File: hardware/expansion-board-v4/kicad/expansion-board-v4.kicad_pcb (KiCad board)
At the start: 6 copper layers, 100 x 62 mm, 174 parts, among them J1 PinHeader_2x20_P2.54mm_Vertic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, J2 U.FL_Hirose_U.FL-R-SMT-1_Vert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, J4 USB_C_Receptacle_HRO_TYPE-C-3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, J5 U.FL_Hirose_U.FL-R-SMT-1_Vert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, J6 U.FL_Hirose_U.FL-R-SMT-1_Vert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, J7 U.FL_Hirose_U.FL-R-SMT-1_Vert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, J8 U.FL_Hirose_U.FL-R-SMT-1_Vert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, J9 MX1.25WT-2P, Q2 SOT-23, Q3 SOT-23, Q4 SOT-23, Q5 SOT-23, SW2 SolderJumper-2_P1.3mm_Open_Pa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, U1 SOT-23-5, U10 QFN-48-1EP_7x7mm_P0.5mm_EP5.1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, U11 DFN-8-1EP_2x2mm_P0.5mm_EP0.86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, U12 SOT-363_SC-70-6, U14 MSOP-8_3x3mm_P0.65mm, U15 SOT-23-6, U16 SOT-363_SC-70-6, U17 SOT-363_SC-70-6, U18 SOIC-10_3.9x4.9mm_P1mm, U19 QFN-24-1EP_4x4mm_P0.5mm_EP2.6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, U2 SOT-23-5, U20 TSOT-23-6, U3 SOT-23-5, U4 BNO085_LGA-28, U5 BMP388_LGA-10, U6 LGA-16_3x3mm_P0.5mm, U7 ATGM336H_LCC-18, U8 QFN-56-1EP_7x7mm_P0.4mm_EP3.2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, U9 SOIC-8_5.3x5.3mm_P1.27mm, Y1 Crystal_SMD_3225-4Pin_3.2x2.5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, Y2 Crystal_SMD_3225-4Pin_3.2x2.5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, Y3 Crystal_SMD_3215-2Pin_3.2x1.5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

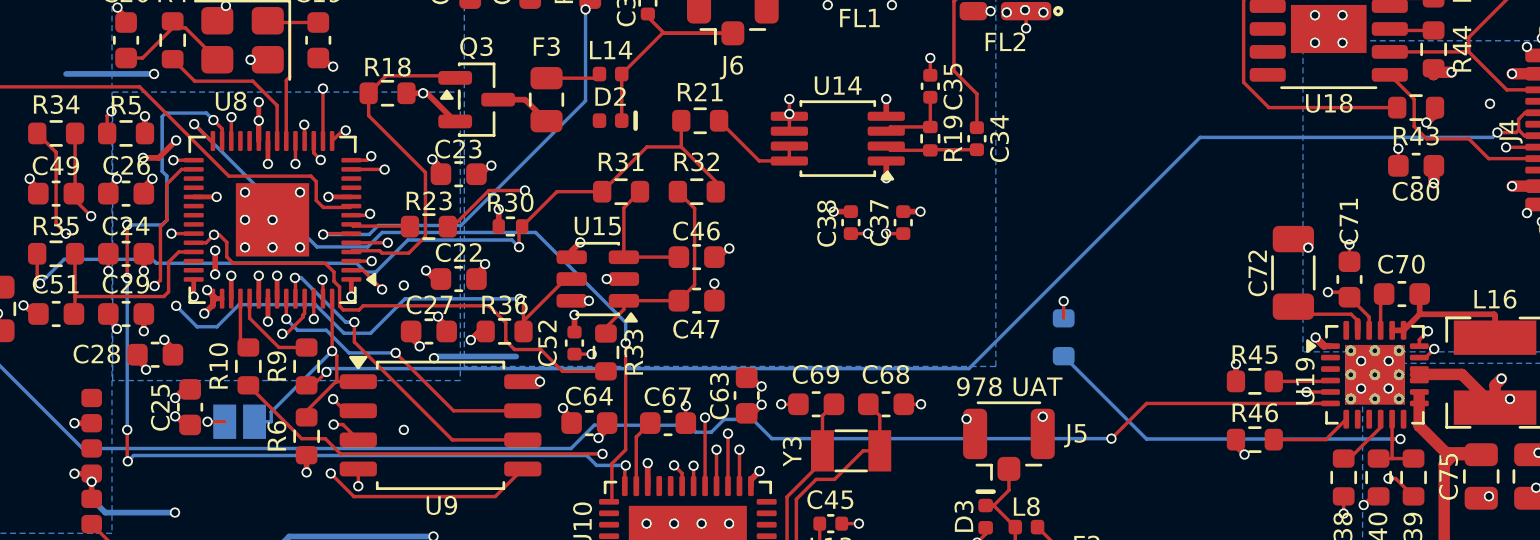
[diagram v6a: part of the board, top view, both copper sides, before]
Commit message: chore(v4): 固化——八维度 1:1 复现通过
从固化数据走完整重建链（gen_pcb → import_routes → route_ifa_feed →
silk_texts → silk_size → gen_polarity_marks → enforce_via_spec），
与手上这块板逐维度比对：

    元件       174 / 174   ✅      覆铜区      15 /  15   ✅
    位号       174 / 174   ✅      板级图元    26 /  26   ✅
    走线      1250 /1250   ✅      封装丝印   174 / 174   ✅
    过孔       385 / 385   ✅      焊盘钻孔   174 / 174   ✅
    未连通       0 /   0   ✅

走线/过孔的差异只有 1~50nm（KiCad 内部单位就是 1nm，制造分辨率是 µm）。

本轮板子改动：
· U19 EP 的 9 个 via-in-pad 钻孔 0.20 → 0.30mm（环宽 0.100mm）
· 删掉我之前多加的 4 个 EP 过孔——9 个 0.3mm 的 3×3 阵列已经够，
  13 个孔挤在 2.6mm EP 里过密
· RP_1V1 两条桥接线按可用上限收到 0.47 / 0.22mm
  （其中一条被 SUBG_RESET 过孔卡死，DRC 报 0.0495mm 间距）
· CHG_PMID 采纳罩哥的 0.25mm
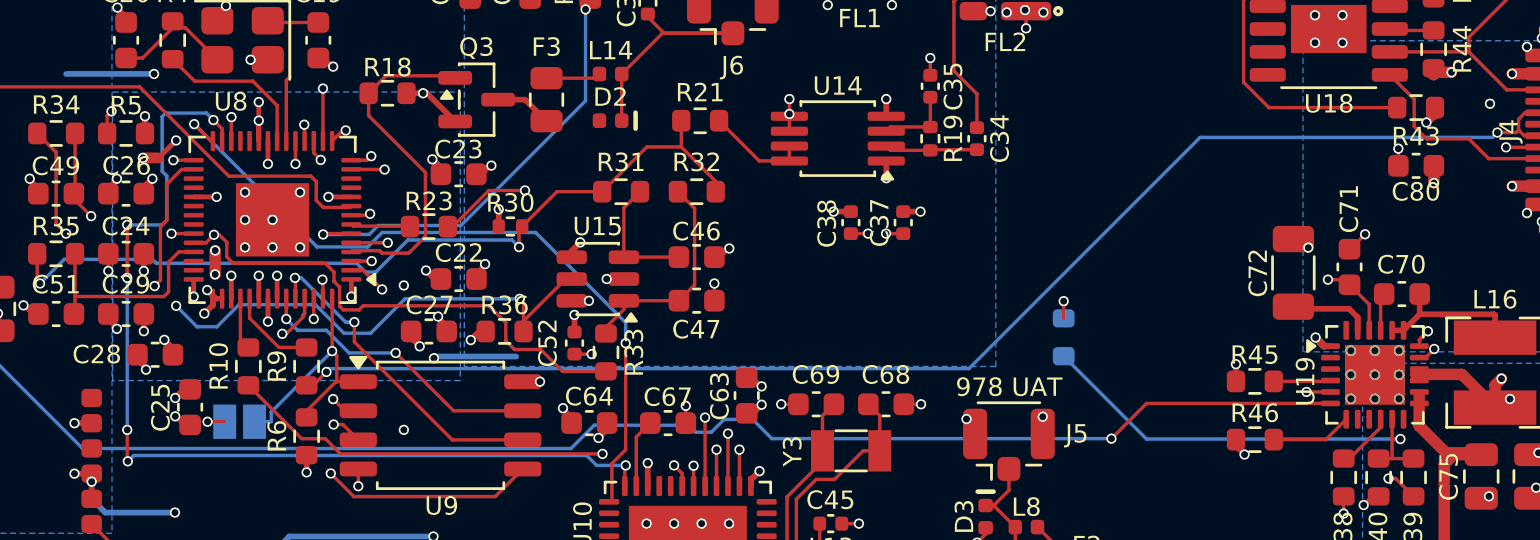
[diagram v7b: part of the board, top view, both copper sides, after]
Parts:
- moved C71 0.55 mm to (133.4, 79.0)
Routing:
- net CHG_REGN: track 13.5 -> 14.2 mm
- net GND: track 139.5 -> 139.7 mm, vias 186 -> 182
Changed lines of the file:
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@@
 			(at -1.05 -1.05)
 			(size 0.5 0.5)
-			(drill 0.2)
+			(drill 0.3)
 			(property pad_prop_heatsink)
 			(layers "*.Cu")
@@
 			(at -1.05 0)
 			(size 0.5 0.5)
-			(drill 0.2)
+			(drill 0.3)
 			(property pad_prop_heatsink)
 			(layers "*.Cu")
@@
 			(at -1.05 1.05)
 			(size 0.5 0.5)
-			(drill 0.2)
+			(drill 0.3)
 			(property pad_prop_heatsink)
 			(layers "*.Cu")
@@
 			(at 0 -1.05)
 			(size 0.5 0.5)
-			(drill 0.2)
+			(drill 0.3)
 			(property pad_prop_heatsink)
 			(layers "*.Cu")
@@
 			(at 0 0)
 			(size 0.5 0.5)
-			(drill 0.2)
+			(drill 0.3)
 			(property pad_prop_heatsink)
 			(layers "*.Cu")
@@
 			(at 0 1.05)
 			(size 0.5 0.5)
-			(drill 0.2)
+			(drill 0.3)
 			(property pad_prop_heatsink)
 			(layers "*.Cu")
@@
 			(at 1.05 -1.05)
 			(size 0.5 0.5)
-			(drill 0.2)
+			(drill 0.3)
 			(property pad_prop_heatsink)
 			(layers "*.Cu")
@@
 			(at 1.05 0)
 			(size 0.5 0.5)
-			(drill 0.2)
+			(drill 0.3)
 			(property pad_prop_heatsink)
 			(layers "*.Cu")
@@
 			(at 1.05 1.05)
 			(size 0.5 0.5)
-			(drill 0.2)
+			(drill 0.3)
 			(property pad_prop_heatsink)
 			(layers "*.Cu")
@@
 	(footprint "C_0603_1608Metric"
 		(layer "F.Cu")
-		(at 133.369 79.521 90)
+		(at 133.369 78.975 90)
 		(descr "Capacitor SMD 0603 (1608 Metric), square (rectangular) end terminal, IPC-7351 nominal, (Body size source: IPC-SM-782 page 76, https://www.pcb-3d.com/wordpress/wp-content/uploads/ipc-sm-782a_amendment_1_and_2.pdf)")
 		(tags "capacitor")
@@
 	)
 	(segment
-		(start 136.416 82.1535)
-		(end 136.79 81.7785)
+		(start 133.4 78.2)
+		(end 134.05 77.55)
 		(width 0.15)
 		(layer "F.Cu")
@@
 	)
 	(segment
-		(start 133.369 78.746)
-		(end 133.369 77.996)
+		(start 136.416 82.1535)
+		(end 136.79 81.7785)
 		(width 0.15)
 		(layer "F.Cu")
@@
 	)
 	(segment
+		(start 133.369 78.2)
+		(end 133.4 78.2)
+		(width 0.15)
+		(layer "F.Cu")
+		(net "GND")
+	)
+	(segment
 		(start 60.96 91.795)
 		(end 60.21 91.795)
@@
 	)
 	(via
-		(at 133.877999 83.078)
-		(size 0.45)
-		(drill 0.3)
-		(layers "F.Cu" "B.Cu")
-		(net "GND")
-	)
-	(via
 		(at 117.714 67.818)
 		(size 0.45)
@@
 	)
 	(via
-		(at 133.877999 84.278)
-		(size 0.45)
-		(drill 0.3)
-		(layers "F.Cu" "B.Cu")
-		(net "GND")
-	)
-	(via
 		(at 106.696 62.858)
 		(size 0.45)
@@
 	)
 	(via
-		(at 133.369 77.996)
+		(at 134.05 77.55)
 		(size 0.45)
 		(drill 0.3)
@@
 	)
 	(via
-		(at 135.078 84.278)
-		(size 0.45)
-		(drill 0.3)
-		(layers "F.Cu" "B.Cu")
-		(net "GND")
-	)
-	(via
 		(at 85.44 69.938)
 		(size 0.45)
@@
 	)
 	(via
-		(at 135.078 83.078)
-		(size 0.45)
-		(drill 0.3)
-		(layers "F.Cu" "B.Cu")
-		(net "GND")
-	)
-	(via
 		(at 101.968 98.31)
 		(size 0.45)
@@
 	)
 	(segment
-		(start 132.4298 80.0747)
-		(end 133.1477 80.0747)
+		(start 134.228 80.609)
+		(end 134.228 81.7405)
 		(width 0.15)
 		(layer "F.Cu")
@@
 	)
 	(segment
-		(start 133.1477 80.0747)
-		(end 133.369 80.296)
+		(start 132.4298 79.5287)
+		(end 133.1477 79.5287)
 		(width 0.15)
 		(layer "F.Cu")
@@
 	)
 	(segment
-		(start 133.369 80.296)
-		(end 134.228 81.155)
-		(width 0.15)
-		(layer "F.Cu")
-		(net "CHG_REGN")
-	)
-	(segment
-		(start 134.228 81.155)
-		(end 134.228 81.7405)
+		(start 133.369 79.75)
+		(end 134.228 80.609)
 		(width 0.15)
 		(layer "F.Cu")
@@
 	)
 	(via
-		(at 132.4298 80.0747)
+		(at 132.4298 79.5287)
 		(size 0.45)
 		(drill 0.3)
@@
 	)
 	(segment
-		(start 132.4298 85.5603)
-		(end 135.0707 88.2012)
+		(start 132.4298 79.5287)
+		(end 132.4298 85.5603)
 		(width 0.15)
 		(layer "In2.Cu")
@@
 	)
 	(segment
-		(start 132.4298 80.0747)
-		(end 132.4298 85.5603)
+		(start 132.4298 85.5603)
+		(end 135.0707 88.2012)
 		(width 0.15)
 		(layer "In2.Cu")
@@
 	)
 	(segment
-		(start 130.922 80.708)
-		(end 131.241999 81.037)
-		(width 0.15)
+		(start 133.35 80.8)
+		(end 133.728 81.178)
+		(width 0.25)
 		(layer "F.Cu")
 		(net "CHG_PMID")
 	)
 	(segment
-		(start 131.241999 81.037)
-		(end 133.437999 81.037)
-		(width 0.15)
+		(start 131.014 80.8)
+		(end 133.35 80.8)
+		(width 0.25)
 		(layer "F.Cu")
 		(net "CHG_PMID")
 	)
 	(segment
-		(start 133.437999 81.037)
-		(end 133.728 81.318)
-		(width 0.15)
+		(start 133.728 81.318)
+		(end 133.728 81.7405)
+		(width 0.26)
 		(layer "F.Cu")
 		(net "CHG_PMID")
 	)
 	(segment
-		(start 133.728 81.318)
-		(end 133.728 81.7405)
-		(width 0.26)
+		(start 130.922 80.708)
+		(end 131.014 80.8)
+		(width 0.25)
+		(layer "F.Cu")
+		(net "CHG_PMID")
+	)
+	(segment
+		(start 133.728 81.178)
+		(end 133.728 81.318)
+		(width 0.25)
 		(layer "F.Cu")
 		(net "CHG_PMID")
@@
 		(start 80.7466 74.2188)
 		(end 81.4324 74.2188)
-		(width 0.25)
+		(width 0.47)
 		(layer "F.Cu")
 		(net "RP_1V1")
@@
 		(start 83.8962 78.2574)
 		(end 83.8962 79.2988)
-		(width 0.25)
+		(width 0.5)
 		(layer "F.Cu")
 		(net "RP_1V1")
@@
 		(start 81.4324 74.2188)
 		(end 82.1944 73.4568)
-		(width 0.25)
+		(width 0.22)
 		(layer "F.Cu")
 		(net "RP_1V1")

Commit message: chore(v4): 固化——含元件值的八维度 1:1 复现通过
    元件(含值)  174 / 174   ✅      覆铜区      15 /  15   ✅
    位号        174 / 174   ✅      板级图元    26 /  26   ✅
    走线       1250 /1250   ✅      封装丝印   174 / 174   ✅
    过孔        385 / 385   ✅      焊盘钻孔   174 / 174   ✅
    未连通        0 /   0   ✅

打板 review 全部通过：
    DRC 零违例 / 未连通 0
    过孔 385 个全 ≥0.3mm 钻孔、≥0.4mm 外径
    射频 103 段全 F.Cu / 0 过孔 / In1 参考面 0 段走线
    最小线宽 0.150 / 最小环宽 0.075 / 孔壁间距 ≥0.25 / 孔到板边 2.70
    Gerber 13 层 + PTH/NPTH 钻孔 + 坐标文件导出正常
    板↔网表：位号无重复、无缺件、封装 170/170、值 170/170
    BATT 极性丝印与 J9 焊盘一致
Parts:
- ANT1: value ANT_IFA_1090MHz -> IFA_1090
- C1, C18, C73, C74, C75: value C_0805_2012Metric -> 10uF
- C10, C11, C12, C13, C14, C16, C17, C22, C23, C24, C25, C26, C27, C49, C61, C62, C63, C64, C65: value C_0603_1608Metric -> 100nF
- C15, C71: value C_0603_1608Metric -> 4.7uF
- C19, C20, C69: value C_0603_1608Metric -> 15pF
- C2, C28, C29, C3, C4, C6, C67, C78, C79, C80: value C_0603_1608Metric -> 1uF
- C30, C38, C39, C45, C53, C54, C57, C58, C59: value C_0402_1005Metric -> 100pF
- C31, C32, C33: value C_0402_1005Metric -> 12pF
- C34, C35, C43: value C_0402_1005Metric -> 3pF
- C37, C52: value C_0402_1005Metric -> 100nF
- C40, C44: value C_0402_1005Metric -> 3.6pF
- C41: value C_0402_1005Metric -> 2.7pF
- C42: value C_0402_1005Metric -> 6.2pF
- C46: value C_0603_1608Metric -> 3pF
- C47: value C_0603_1608Metric -> 200pF
- C5: value C_0402_1005Metric -> 1uF
- C51: value C_0603_1608Metric -> 1nF
- C55, C56: value C_0603_1608Metric -> 100pF
- C60, C66: value C_0805_2012Metric -> 22uF
- C68: value C_0603_1608Metric -> 12pF
- C70: value C_0603_1608Metric -> 47nF
- C72: value C_1206_3216Metric -> 6.8uF
- C76, C77: value C_1206_3216Metric -> 22uF
- D2, D3: value D_0402_1005Metric -> ESD 3.3V/0.6pF
- F2, F3, F4, F5: value Fuse_0805_2012Metric -> 6V/200mA
- FL1, FL2: value TA0970A_SMD3838-6 -> TA0970A
- J1: value PinHeader_2x20_P2.54mm_Vertical_SMD -> J3_HAT_2x20_SMD排针
- J2: value U.FL_Hirose_U.FL-R-SMT-1_Vertical -> U.FL_GNSS_EXT(经尾线转SMA)
- J4: value USB_C_Receptacle_HRO_TYPE-C-31-M-12 -> USB-C_16P
- J5: value U.FL_Hirose_U.FL-R-SMT-1_Vertical -> U.FL_978
- J6: value U.FL_Hirose_U.FL-R-SMT-1_Vertical -> U.FL_1090_EXT(经尾线转SMA)
- J7: value U.FL_Hirose_U.FL-R-SMT-1_Vertical -> U.FL_IFA_TEST(π后调试口)
- J8: value U.FL_Hirose_U.FL-R-SMT-1_Vertical -> U.FL→内置patch
- J9: value MX1.25WT-2P -> MX1.25WT-2P BAT
- L10: value L_0402_1005Metric -> 27nH
- L11, L12: value L_0402_1005Metric -> 6.8nH
- L13, L9: value L_0402_1005Metric -> 7.5nH
- L14, L8: value L_0402_1005Metric -> 100nH
- L15, L2: value L_0402_1005Metric -> 33nH
- L16: value L_Bourns-SRN4018 -> 1uH
- L17: value L_Bourns-SRN4018 -> 1.5uH
- L7: value L_0805_2012Metric -> 6.8uH
- Q2, Q3, Q4, Q5: value SOT-23 -> AO3401A
- R1, R17, R18, R26, R27, R32, R34, R35, R44, R45, R46, R5, R6: value R_0603_1608Metric -> 10k
- R10, R9: value R_0603_1608Metric -> 27R
- R19: value R_0402_1005Metric -> 52.3R
- R2, R3: value R_0603_1608Metric -> 4.7k
- R21, R22, R23: value R_0603_1608Metric -> 0R
- R24: value R_0402_1005Metric -> 0R DNP(旁路外接)
- R25: value R_0402_1005Metric -> 0R DNP(旁路板载)
- R30: value R_0402_1005Metric -> 1k
- R31, R36, R4, R43: value R_0603_1608Metric -> 1k
- R33: value R_0603_1608Metric -> 100k
- R37: value R_0603_1608Metric -> 6.8k
- R38: value R_0603_1608Metric -> 180R
- R39: value R_0603_1608Metric -> 5.62k
- R40: value R_0603_1608Metric -> 31.6k
- R41: value R_0603_1608Metric -> 470k
- R42: value R_0603_1608Metric -> 150k
- R7, R8: value R_0603_1608Metric -> 5.1k
- RT1: value R_0603_1608Metric -> NCP18XH103F03RB 10k NTC
- SW2: value SolderJumper-2_P1.3mm_Open_Pad1.0x1.5mm -> BOOTSEL短接焊盘
- U1: value SOT-23-5 -> ME6211C33M5
- U10: value QFN-48-1EP_7x7mm_P0.5mm_EP5.15x5.15mm -> CC1312R1F3RGZR
- U11: value DFN-8-1EP_2x2mm_P0.5mm_EP0.86x1.55mm -> QPL9547TR7
- U12: value SOT-363_SC-70-6 -> BGA2817
- U14: value MSOP-8_3x3mm_P0.65mm -> AD8313ARMZ
- U15: value SOT-23-6 -> TLV3501(TOKMAS)
- U16, U17: value SOT-363_SC-70-6 -> XA17-G4K(或AS179-92LF)
- U18: value SOIC-10_3.9x4.9mm_P1mm -> CH224K
- U19: value QFN-24-1EP_4x4mm_P0.5mm_EP2.6x2.6mm_ThermalVias -> SY6970
- U2, U3: value SOT-23-5 -> TPS7A2033PDBVR
- U20: value TSOT-23-6 -> SY7069
- U4: value BNO085_LGA-28 -> BNO085
- U5: value BMP388_LGA-10 -> BMP388
- U6: value LGA-16_3x3mm_P0.5mm -> QMC5883P
- U7: value ATGM336H_LCC-18 -> ATGM336H-6N-74
- U8: value QFN-56-1EP_7x7mm_P0.4mm_EP3.2x3.2mm -> RP2040
- U9: value SOIC-8_5.3x5.3mm_P1.27mm -> W25Q128JVSIQ
- Y1: value Crystal_SMD_3225-4Pin_3.2x2.5mm -> 12MHz
- Y2: value Crystal_SMD_3225-4Pin_3.2x2.5mm -> 48MHz ABM8W-7pF
- Y3: value Crystal_SMD_3215-2Pin_3.2x1.5mm -> 32.768kHz FC-135
- ZP1: value C_0603_1608Metric -> DNP 并-天线侧
- ZP2: value C_0603_1608Metric -> DNP 并-电台侧
- ZS1: value L_0603_1608Metric -> 0R 串
